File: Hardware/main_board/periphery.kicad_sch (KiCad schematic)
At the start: 66 parts, among them J4 SD, J5 NFC, J6 EXT1, J7 EXT0, U12 LP5562TMX

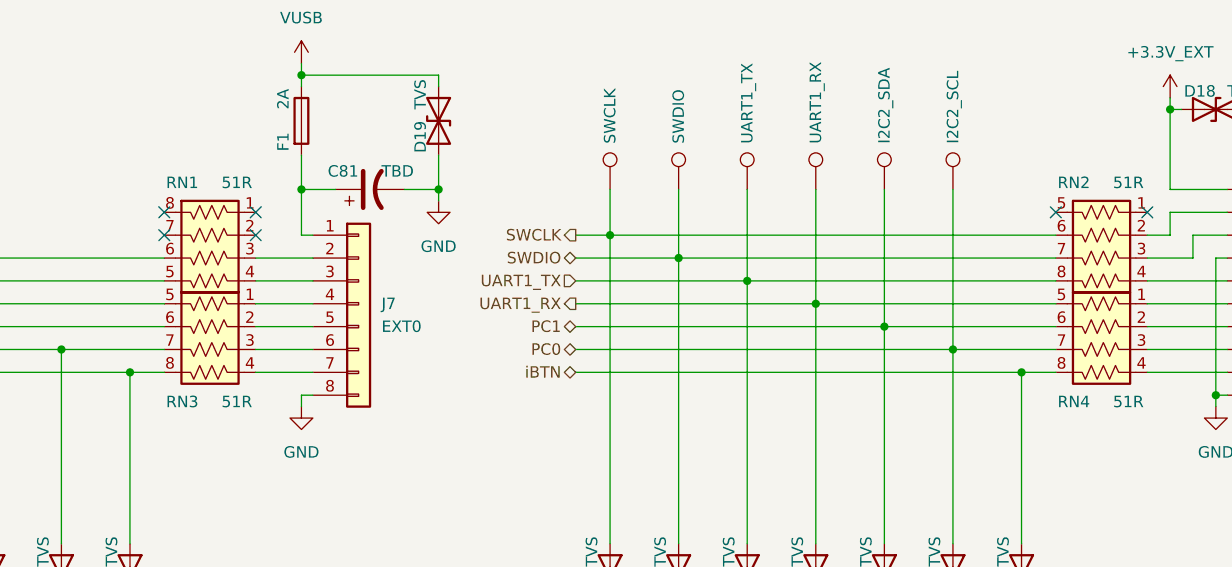
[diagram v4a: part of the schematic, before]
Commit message: sch: fix wrong symbol
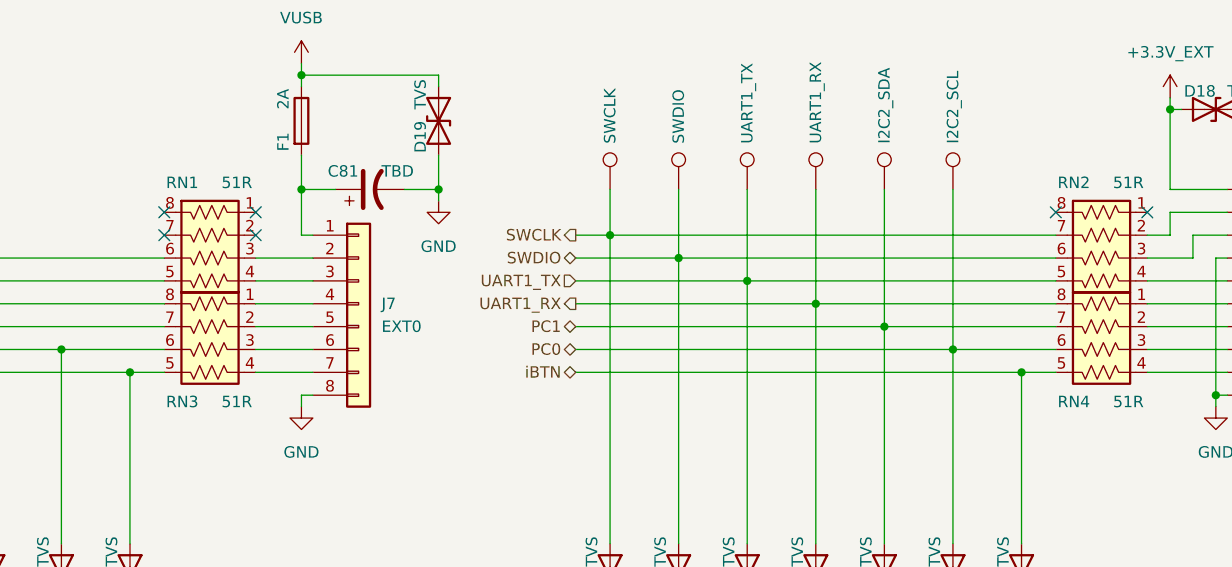
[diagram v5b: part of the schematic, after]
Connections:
- net PA4: now also RN3.8; no longer RN3.5
- net PB2: now also RN3.6; no longer RN3.7
- net PB3: now also RN3.7; no longer RN3.6
- net PC0: now also RN4.6; no longer RN4.7
- net PC1: now also RN4.7; no longer RN4.6
- net PC3: now also RN3.5; no longer RN3.8
- net SWCLK: now also RN2.7; no longer RN2.6
- net SWDIO: now also RN2.6; no longer RN2.7
- net UART1_RX: now also RN4.8; no longer RN4.5
- net UART1_TX: now also RN2.5; no longer RN2.8
- net iBTN: now also RN4.5; no longer RN4.8
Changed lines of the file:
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@@
 	)
 	(symbol
-		(lib_name "R_Park_1")
 		(lib_id "Library:R_Park")
 		(at 73.66 130.81 90)

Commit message: sch: change some footprints
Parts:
- J4: footprint Library:TF_C393941 -> Library:TF-101A-P3
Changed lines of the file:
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@@
 			)
 		)
-		(property "Footprint" "Library:TF_C393941"
+		(property "Footprint" "Library:TF-101A-P3"
 			(at 292.1 34.29 0)
 			(effects
@@
 			)
 		)
-		(property "Datasheet" "https://datasheet.lcsc.com/lcsc/2110151630_XKB-Connectivity-XKTF-015-N_C381082.pdf"
+		(property "Datasheet" ""
 			(at 240.03 49.53 0)
 			(effects
@@
 			)
 		)
-		(property "Description" "Micro SD Card Socket with one card detection pin"
+		(property "Description" ""
 			(at 240.03 52.07 0)
 			(effects
